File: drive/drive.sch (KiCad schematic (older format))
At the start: 36 parts, among them J1 MOTOR, J2 28V~~, J3 CAN, J4 AVR-ISP-6, Q2 2N7002, Q3 BTA06-600TW, U1 LM317LI, U2 MCP2551-I-SN, U3 ATmega32M1-AU, Y1 16MHz

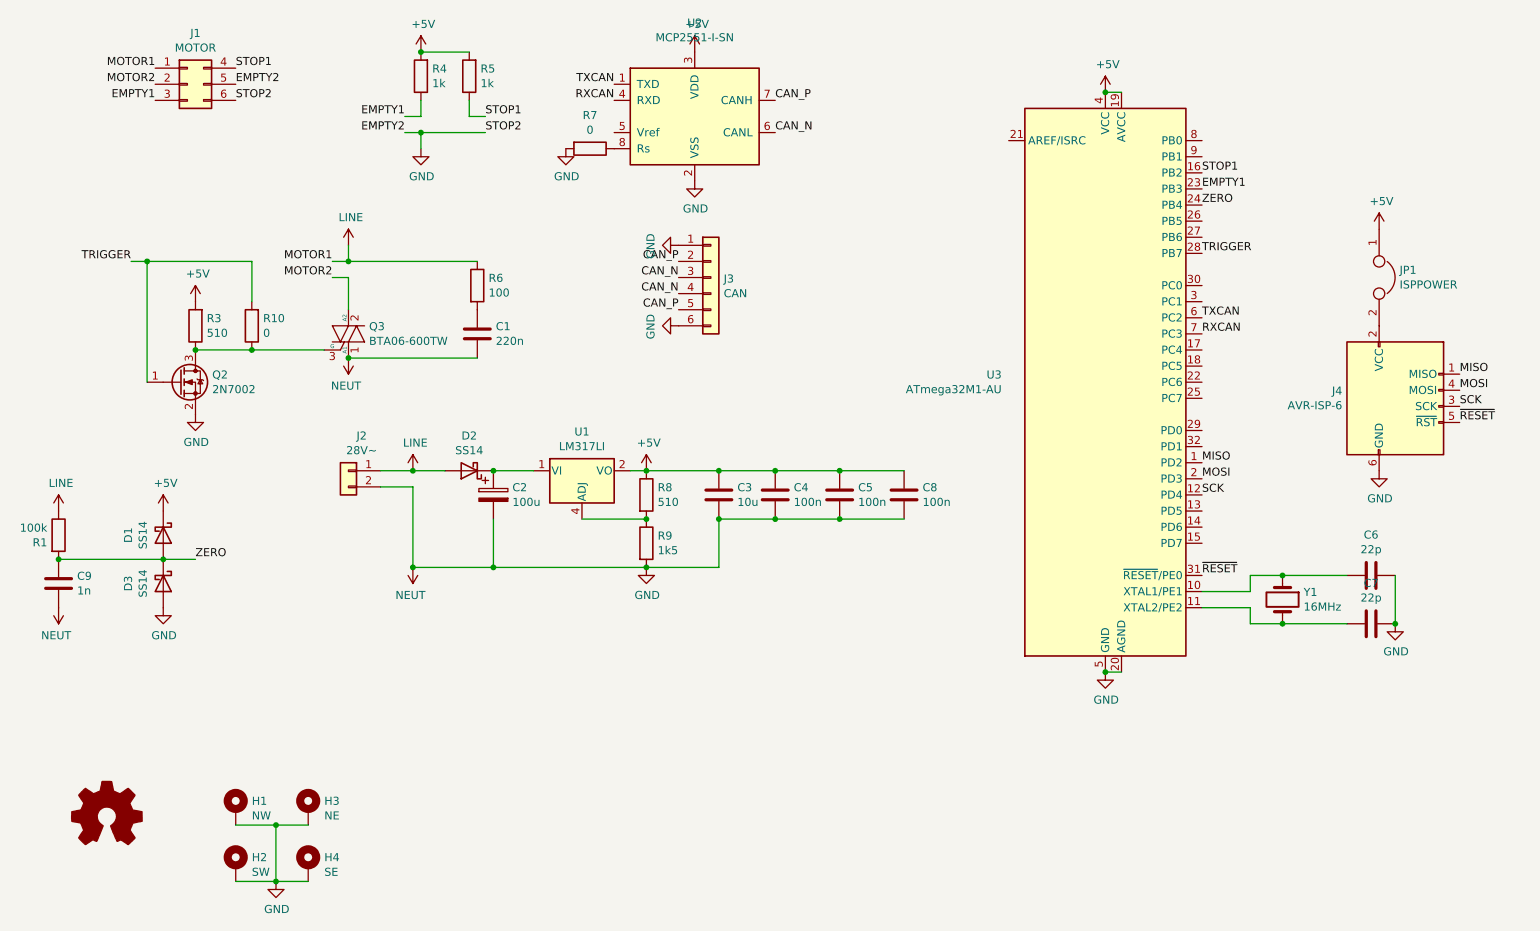
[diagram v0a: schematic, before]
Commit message: drive: optimized routing and power plance placement
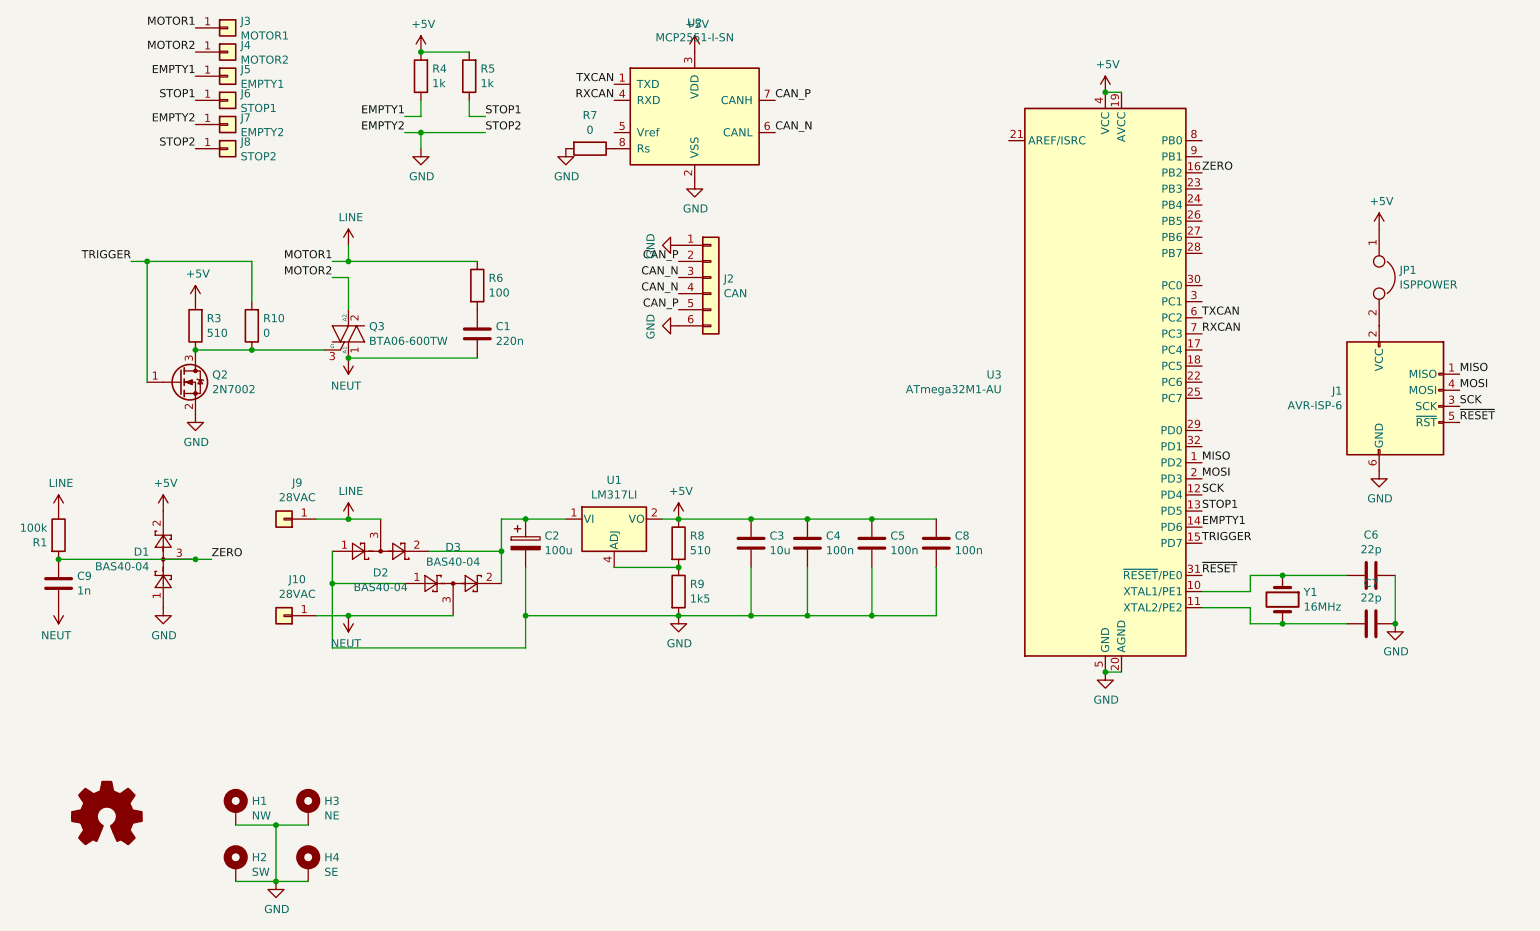
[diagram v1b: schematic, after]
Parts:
- removed D1, D2, D3: SS14, Diode_SMD:D_SMA_Handsoldering, symbol Device:D_Schottky
- removed J1: MOTOR, Connector_PinHeader_2.54mm:PinHeader_2x03_P2.54mm_Vertical, symbol Connector_Generic:Conn_02x03_Top_Bottom
- removed J2: 28V~~, Connector_PinHeader_2.54mm:PinHeader_1x02_P2.54mm_Vertical, symbol Connector_Generic:Conn_01x02
- added D1, D2, D3: BAS40-04, Package_TO_SOT_SMD:SOT-23, symbol Diode:BAS40-04
- added J10, J9: 28VAC, Connector_Pin:Pin_D1.1mm_L10.2mm_W3.5mm_Flat, symbol Connector_Generic:Conn_01x01
- added J3: MOTOR1, Connector_Pin:Pin_D1.1mm_L10.2mm_W3.5mm_Flat, symbol Connector_Generic:Conn_01x01
- added J4: MOTOR2, Connector_Pin:Pin_D1.1mm_L10.2mm_W3.5mm_Flat, symbol Connector_Generic:Conn_01x01
- added J5: EMPTY1, Connector_Pin:Pin_D1.1mm_L10.2mm_W3.5mm_Flat, symbol Connector_Generic:Conn_01x01
- added J6: STOP1, Connector_Pin:Pin_D1.1mm_L10.2mm_W3.5mm_Flat, symbol Connector_Generic:Conn_01x01
- added J7: EMPTY2, Connector_Pin:Pin_D1.1mm_L10.2mm_W3.5mm_Flat, symbol Connector_Generic:Conn_01x01
- added J8: STOP2, Connector_Pin:Pin_D1.1mm_L10.2mm_W3.5mm_Flat, symbol Connector_Generic:Conn_01x01
- R6: footprint Resistor_THT:R_Axial_DIN0207_L6.3mm_D2.5mm_P10.16mm_Horizontal -> Resistor_THT:R_Axial_DIN0207_L6.3mm_D2.5mm_P7.62mm_Horizontal
- renumbered J4 to J1, J3 to J2
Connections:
- net +5V: now also D1.2
- net EMPTY1: now also U3.14 (PD6), J5.1 (Pin_1); no longer U3.23 (PB3)
- net GND: now also D1.1, D2.1, D3.1, J7.1 (Pin_1), J8.1 (Pin_1); no longer C1.2, C9.2, Q3.1 (A1)
- net LINE: now also D2.3, J3.1 (Pin_1), J9.1 (Pin_1)
- net MOTOR2: now also J4.1 (Pin_1)
- net STOP1: now also U3.13 (PD5), J6.1 (Pin_1); no longer U3.16 (PB2)
- net TRIGGER: now also U3.15 (PD7); no longer U3.28 (PB7)
- net ZERO: now also U3.16 (PB2), D1.3; no longer U3.24 (PB4)
- net at C2.1, U1.1 (VI): now also D2.2, D3.2
- new net NEUT: C1.2, C9.2, D3.3, J10.1 (Pin_1), Q3.1 (A1)
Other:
- moved on the sheet: C2, C3, C4, C5, C8, R8, R9, U1

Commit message: Replace power pins with mini-fit jr
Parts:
- removed J10, J9: 28VAC, Connector_Pin:Pin_D1.1mm_L10.2mm_W3.5mm_Flat, symbol Connector_Generic:Conn_01x01
- removed J3: MOTOR1, Connector_Pin:Pin_D1.1mm_L10.2mm_W3.5mm_Flat, symbol Connector_Generic:Conn_01x01
- removed J4: MOTOR2, Connector_Pin:Pin_D1.1mm_L10.2mm_W3.5mm_Flat, symbol Connector_Generic:Conn_01x01
- removed J5: EMPTY1, Connector_Pin:Pin_D1.1mm_L10.2mm_W3.5mm_Flat, symbol Connector_Generic:Conn_01x01
- removed J6: STOP1, Connector_Pin:Pin_D1.1mm_L10.2mm_W3.5mm_Flat, symbol Connector_Generic:Conn_01x01
- removed J7: EMPTY2, Connector_Pin:Pin_D1.1mm_L10.2mm_W3.5mm_Flat, symbol Connector_Generic:Conn_01x01
- removed J8: STOP2, Connector_Pin:Pin_D1.1mm_L10.2mm_W3.5mm_Flat, symbol Connector_Generic:Conn_01x01
- added J11: Power, Connector_Molex:Molex_Mini-Fit_Jr_5569-08A2_2x04_P4.20mm_Horizontal, symbol Connector_Generic:Conn_02x04_Top_Bottom
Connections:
- net EMPTY1: now also J11.7 (Pin_7)
- net GND: now also J11.3 (Pin_3), J11.4 (Pin_4)
- net LINE: now also J11.1 (Pin_1), J11.2 (Pin_2)
- net MOTOR2: now also J11.5 (Pin_5)
- net NEUT: now also J11.6 (Pin_6)
- net STOP1: now also J11.8 (Pin_8)
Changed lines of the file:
@@
 $EndComp
-Wire Wire Line
-	2800 4700 3000 4700
 Wire Wire Line
 	4100 4700 4350 4700
@@
 L power:LINE #PWR08
 U 1 1 5F43C5FC
-P 3000 4700
-F 0 "#PWR08" H 3000 4550 50  0001 C CNN
-F 1 "LINE" H 3015 4873 50  0000 C CNN
-F 2 "" H 3000 4700 50  0001 C CNN
-F 3 "" H 3000 4700 50  0001 C CNN
-	1    3000 4700
+P 2800 4700
+F 0 "#PWR08" H 2800 4550 50  0001 C CNN
+F 1 "LINE" H 2815 4873 50  0000 C CNN
+F 2 "" H 2800 4700 50  0001 C CNN
+F 3 "" H 2800 4700 50  0001 C CNN
+	1    2800 4700
 	1    0    0    -1
 $EndComp
@@
 	1    0    0    -1
 $EndComp
-Wire Wire Line
-	3200 4700 3000 4700
-Connection ~ 3000 4700
 $Comp
 L Connector:AVR-ISP-6 J1
@@
 L power:NEUT #PWR09
 U 1 1 5F43CFFA
-P 3000 5300
-F 0 "#PWR09" H 3000 5150 50  0001 C CNN
-F 1 "NEUT" H 3015 5473 50  0000 C CNN
-F 2 "" H 3000 5300 50  0001 C CNN
-F 3 "" H 3000 5300 50  0001 C CNN
-	1    3000 5300
+P 2800 5300
+F 0 "#PWR09" H 2800 5150 50  0001 C CNN
+F 1 "NEUT" H 2815 5473 50  0000 C CNN
+F 2 "" H 2800 5300 50  0001 C CNN
+F 3 "" H 2800 5300 50  0001 C CNN
+	1    2800 5300
 	-1   0    0    1
 $EndComp
@@
 	-1   0    0    1
 $EndComp
-Text Label 2150 4950 0    50   ~ 0
-ZERO
 Text Label 8300 4850 0    50   ~ 0
 TRIGGER
-$Comp
-L Connector_Generic:Conn_01x01 J3
-U 1 1 5F92A3C9
-P 2250 1650
-F 0 "J3" H 2330 1692 50  0000 L CNN
-F 1 "MOTOR1" H 2330 1601 50  0000 L CNN
-F 2 "Connector_Pin:Pin_D1.1mm_L10.2mm_W3.5mm_Flat" H 2250 1650 50  0001 C CNN
-F 3 "~" H 2250 1650 50  0001 C CNN
-	1    2250 1650
-	1    0    0    -1
-$EndComp
-$Comp
-L Connector_Generic:Conn_01x01 J4
-U 1 1 5F92A98D
-P 2250 1800
-F 0 "J4" H 2330 1842 50  0000 L CNN
-F 1 "MOTOR2" H 2330 1751 50  0000 L CNN
-F 2 "Connector_Pin:Pin_D1.1mm_L10.2mm_W3.5mm_Flat" H 2250 1800 50  0001 C CNN
-F 3 "~" H 2250 1800 50  0001 C CNN
-	1    2250 1800
-	1    0    0    -1
-$EndComp
-$Comp
-L Connector_Generic:Conn_01x01 J5
-U 1 1 5F92ACB1
-P 2250 1950
-F 0 "J5" H 2330 1992 50  0000 L CNN
-F 1 "EMPTY1" H 2330 1901 50  0000 L CNN
-F 2 "Connector_Pin:Pin_D1.1mm_L10.2mm_W3.5mm_Flat" H 2250 1950 50  0001 C CNN
-F 3 "~" H 2250 1950 50  0001 C CNN
-	1    2250 1950
-	1    0    0    -1
-$EndComp
-$Comp
-L Connector_Generic:Conn_01x01 J8
-U 1 1 5F92BDC9
-P 2250 2400
-F 0 "J8" H 2330 2442 50  0000 L CNN
-F 1 "STOP2" H 2330 2351 50  0000 L CNN
-F 2 "Connector_Pin:Pin_D1.1mm_L10.2mm_W3.5mm_Flat" H 2250 2400 50  0001 C CNN
-F 3 "~" H 2250 2400 50  0001 C CNN
-	1    2250 2400
-	1    0    0    -1
-$EndComp
-$Comp
-L Connector_Generic:Conn_01x01 J7
-U 1 1 5F946B1D
-P 2250 2250
-F 0 "J7" H 2330 2292 50  0000 L CNN
-F 1 "EMPTY2" H 2330 2201 50  0000 L CNN
-F 2 "Connector_Pin:Pin_D1.1mm_L10.2mm_W3.5mm_Flat" H 2250 2250 50  0001 C CNN
-F 3 "~" H 2250 2250 50  0001 C CNN
-	1    2250 2250
-	1    0    0    -1
-$EndComp
-$Comp
-L Connector_Generic:Conn_01x01 J6
-U 1 1 5F946D85
-P 2250 2100
-F 0 "J6" H 2330 2142 50  0000 L CNN
-F 1 "STOP1" H 2330 2051 50  0000 L CNN
-F 2 "Connector_Pin:Pin_D1.1mm_L10.2mm_W3.5mm_Flat" H 2250 2100 50  0001 C CNN
-F 3 "~" H 2250 2100 50  0001 C CNN
-	1    2250 2100
-	1    0    0    -1
-$EndComp
-Text Label 2050 1650 2    50   ~ 0
-MOTOR1
-Text Label 2050 1800 2    50   ~ 0
-MOTOR2
-Text Label 2050 1950 2    50   ~ 0
-EMPTY1
-Text Label 2050 2100 2    50   ~ 0
-STOP1
-Text Label 2050 2250 2    50   ~ 0
-EMPTY2
-Text Label 2050 2400 2    50   ~ 0
-STOP2
-$Comp
-L Connector_Generic:Conn_01x01 J9
-U 1 1 5F95D62C
-P 2600 4700
-F 0 "J9" H 2518 4475 50  0000 C CNN
-F 1 "28VAC" H 2518 4566 50  0000 C CNN
-F 2 "Connector_Pin:Pin_D1.1mm_L10.2mm_W3.5mm_Flat" H 2600 4700 50  0001 C CNN
-F 3 "~" H 2600 4700 50  0001 C CNN
-	1    2600 4700
-	-1   0    0    1
-$EndComp
-$Comp
-L Connector_Generic:Conn_01x01 J10
-U 1 1 5F95DC76
-P 2600 5300
-F 0 "J10" H 2518 5075 50  0000 C CNN
-F 1 "28VAC" H 2518 5166 50  0000 C CNN
-F 2 "Connector_Pin:Pin_D1.1mm_L10.2mm_W3.5mm_Flat" H 2600 5300 50  0001 C CNN
-F 3 "~" H 2600 5300 50  0001 C CNN
-	1    2600 5300
-	-1   0    0    1
-$EndComp
 $Comp
 L Diode:BAS40-04 D1
@@
 	0    -1   -1   0
 $EndComp
-Wire Wire Line
-	2050 4950 1200 4950
 Connection ~ 1200 4950
-Wire Wire Line
-	2150 4950 2050 4950
-Connection ~ 2050 4950
 $Comp
 L Diode:BAS40-04 D2
@@
 Connection ~ 4100 5300
 Wire Wire Line
-	2800 5300 3000 5300
-Connection ~ 3000 5300
-Wire Wire Line
-	3000 5300 3650 5300
-Wire Wire Line
 	2900 5100 2900 5500
+$Comp
+L Connector_Generic:Conn_02x04_Top_Bottom J11
+U 1 1 5FD23FC4
+P 1900 2050
+F 0 "J11" H 1950 2367 50  0000 C CNN
+F 1 "Power" H 1950 2276 50  0000 C CNN
+F 2 "Connector_Molex:Molex_Mini-Fit_Jr_5569-08A2_2x04_P4.20mm_Horizontal" H 1900 2050 50  0001 C CNN
+F 3 "~" H 1900 2050 50  0001 C CNN
+	1    1900 2050
+	1    0    0    -1
+$EndComp
+Text Label 1700 1950 2    50   ~ 0
+MOTOR1
+Text Label 2200 1950 0    50   ~ 0
+MOTOR2
+Text Label 2200 2150 0    50   ~ 0
+EMPTY1
+Text Label 2200 2250 0    50   ~ 0
+STOP1
+Text Label 1700 2150 2    50   ~ 0
+EMPTY2
+Text Label 1700 2250 2    50   ~ 0
+STOP2
+Wire Wire Line
+	1600 2050 1700 2050
+$Comp
+L power:LINE #PWR0108
+U 1 1 5FD2758F
+P 1600 1850
+F 0 "#PWR0108" H 1600 1700 50  0001 C CNN
+F 1 "LINE" H 1615 2023 50  0000 C CNN
+F 2 "" H 1600 1850 50  0001 C CNN
+F 3 "" H 1600 1850 50  0001 C CNN
+	1    1600 1850
+	1    0    0    -1
+$EndComp
+Wire Wire Line
+	1600 1850 1600 2050
+Wire Wire Line
+	2300 2050 2200 2050
+$Comp
+L power:NEUT #PWR0109
+U 1 1 5FD278FC
+P 2300 2300
+F 0 "#PWR0109" H 2300 2150 50  0001 C CNN
+F 1 "NEUT" H 2315 2473 50  0000 C CNN
+F 2 "" H 2300 2300 50  0001 C CNN
+F 3 "" H 2300 2300 50  0001 C CNN
+	1    2300 2300
+	-1   0    0    1
+$EndComp
+Wire Wire Line
+	2300 2300 2300 2050
+Text Label 2150 4950 0    50   ~ 0
+ZERO
+Wire Wire Line
+	2150 4950 2050 4950
+Wire Wire Line
+	2050 4950 1200 4950
+Connection ~ 2050 4950
+Wire Wire Line
+	2800 5300 3650 5300
+Wire Wire Line
+	2800 4700 3200 4700
 $EndSCHEMATC

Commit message: Replaced BAS-40 with BAS-70 to avoid peak-peak overvoltage
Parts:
- D1, D2, D3: value BAS40-04 -> BAS70-04
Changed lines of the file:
@@
 Text Label 8300 4850 0    50   ~ 0
 TRIGGER
-$Comp
-L Diode:BAS40-04 D1
-U 1 1 5F96F94B
-P 1950 4950
-F 0 "D1" V 1996 5137 50  0000 L CNN
-F 1 "BAS40-04" V 1905 5137 50  0000 L CNN
-F 2 "Package_TO_SOT_SMD:SOT-23" H 1700 5250 50  0001 L CNN
-F 3 "http://www.vishay.com/docs/85701/bas40v.pdf" H 1830 5050 50  0001 C CNN
-	1    1950 4950
-	0    -1   -1   0
-$EndComp
 Connection ~ 1200 4950
 $Comp
@@
 P 3200 4800
 F 0 "D2" H 3200 5033 50  0000 C CNN
-F 1 "BAS40-04" H 3200 5124 50  0000 C CNN
+F 1 "BAS70-04" H 3200 5124 50  0000 C CNN
 F 2 "Package_TO_SOT_SMD:SOT-23" H 2950 5100 50  0001 L CNN
 F 3 "http://www.vishay.com/docs/85701/bas40v.pdf" H 3080 4900 50  0001 C CNN
@@
 P 3650 5200
 F 0 "D3" H 3650 5525 50  0000 C CNN
-F 1 "BAS40-04" H 3650 5434 50  0000 C CNN
+F 1 "BAS70-04" H 3650 5434 50  0000 C CNN
 F 2 "Package_TO_SOT_SMD:SOT-23" H 3400 5500 50  0001 L CNN
 F 3 "http://www.vishay.com/docs/85701/bas40v.pdf" H 3530 5300 50  0001 C CNN
@@
 ZERO
 Wire Wire Line
-	2150 4950 2050 4950
-Wire Wire Line
-	2050 4950 1200 4950
-Connection ~ 2050 4950
-Wire Wire Line
 	2800 5300 3650 5300
 Wire Wire Line
 	2800 4700 3200 4700
+Wire Wire Line
+	2050 4950 1200 4950
+Wire Wire Line
+	2150 4950 2050 4950
+Connection ~ 2050 4950
+$Comp
+L Diode:BAS40-04 D1
+U 1 1 5F96F94B
+P 1950 4950
+F 0 "D1" V 1996 5137 50  0000 L CNN
+F 1 "BAS70-04" V 1905 5137 50  0000 L CNN
+F 2 "Package_TO_SOT_SMD:SOT-23" H 1700 5250 50  0001 L CNN
+F 3 "http://www.vishay.com/docs/85701/bas40v.pdf" H 1830 5050 50  0001 C CNN
+	1    1950 4950
+	0    -1   -1   0
+$EndComp
 $EndSCHEMATC
